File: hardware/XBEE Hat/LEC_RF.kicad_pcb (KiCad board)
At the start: 2 copper layers, 70 x 40 mm, 6 parts, among them J1 Conn_Coaxial_Small, J2 Conn_01x04, U1 XBee_SMT, U2 TLV1117-33

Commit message: Push of most recent schematic and PCB
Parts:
- C1, C2: footprint Capacitor_SMD:C_0805_2012Metric -> Capacitor_SMD:C_0603_1608Metric
- U1: footprint RF_Module:Digi_XBee_SMT -> Custom:XBEE_GND_PAD
- moved J2 11.1 mm to (84.3, 85.0)
- moved U2 10.3 mm to (86.0, 66.0)
- moved C1 2.70 mm to (125.2, 62.0)
- moved C2 2.00 mm to (128.1, 62.0)
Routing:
- net UART_TX: track 0.00 -> 51.1 mm, vias 0 -> 1
- net UART_RX: track 0.00 -> 47.4 mm
- net +3.3V: track 9.13 -> 54.2 mm
- net +5V: track 0.00 -> 9.89 mm
- net Net-(J1-In): track 0.00 -> 7.13 mm
- added copper zone on B.Cu, net GND
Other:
- board size 70 x 40 mm -> 60 x 40 mm

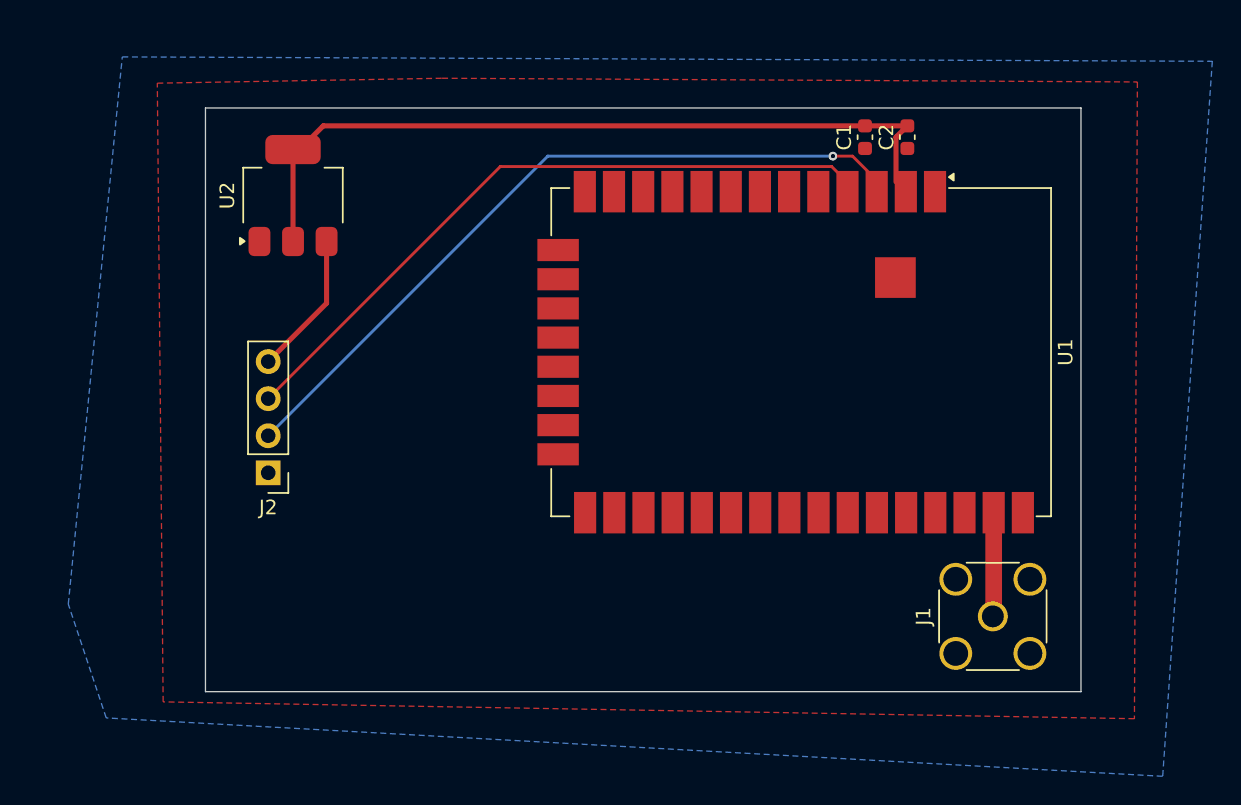
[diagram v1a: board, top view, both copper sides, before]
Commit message: Routed XBEE PCB
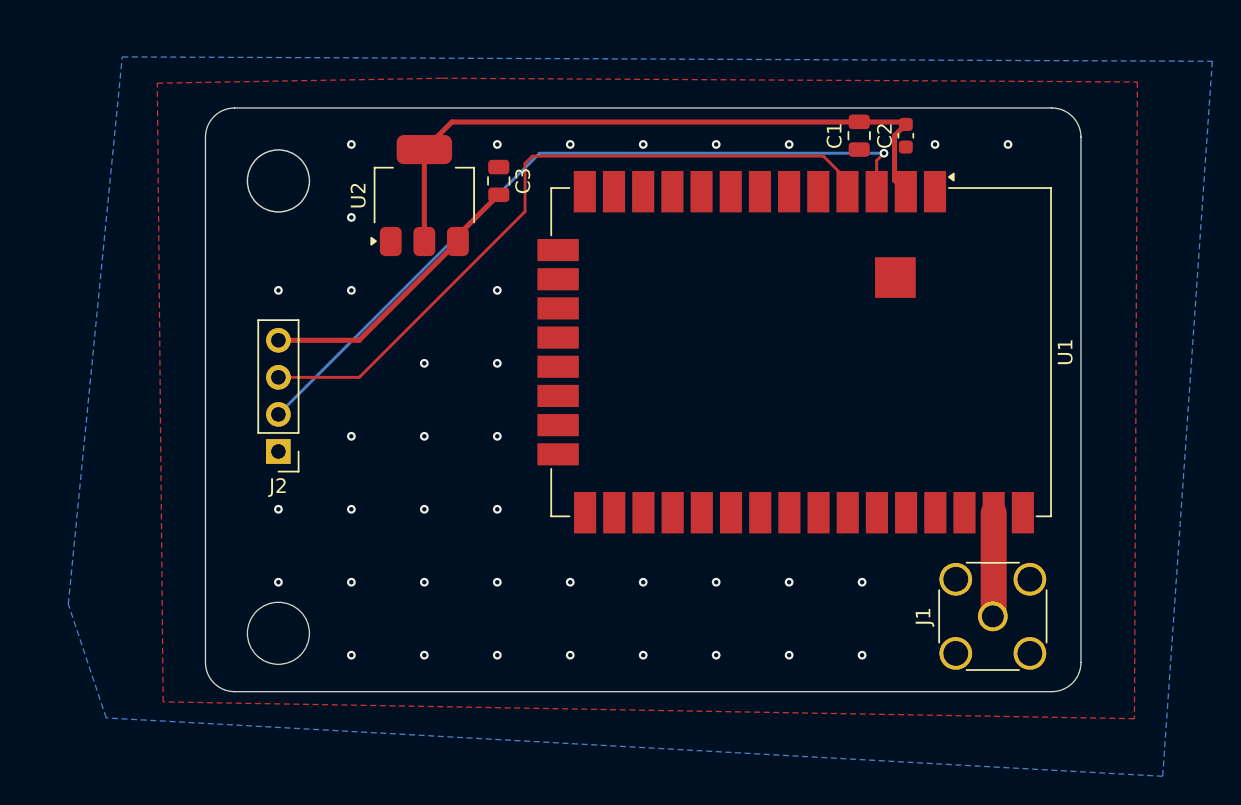
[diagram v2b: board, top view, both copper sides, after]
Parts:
- added C3: 1uF, Capacitor_SMD:C_0805_2012Metric, F.Cu at (100.1, 65.0)
- C1: footprint Capacitor_SMD:C_0603_1608Metric -> Capacitor_SMD:C_0805_2012Metric
- U2: value TLV1117-33 -> TLV1117LV33DCYR
- moved U2 9.00 mm to (95.0, 66.0)
- moved J2 1.62 mm to (85.0, 83.5)
- moved C1 0.41 mm to (124.8, 61.9)
- moved C2 0.14 mm to (128.0, 61.9)
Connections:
- net UART_RX renamed /UART_RX
- net UART_TX renamed /UART_TX
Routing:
- net +5V: track 9.89 -> 19.5 mm
- net +3.3V: track 54.2 -> 45.4 mm
- net /UART_RX: track 47.4 -> 48.7 mm
- net /UART_TX: track 51.1 -> 51.8 mm
- net GND: vias 0 -> 38
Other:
- outline, holes or cut-outs redrawn

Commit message: Final revision of XBEE board
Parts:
- removed J1: Conn_Coaxial_Small, Connector_Coaxial:SMA_Wurth_60312002114503_Vertical
- added C4: 1nF, Capacitor_SMD:C_0805_2012Metric, F.Cu at (117.5, 62.2)
- added R1: 300, Resistor_SMD:R_0805_2012Metric, F.Cu at (112.8, 62.2)
- added REF**: MountingHole_3.2mm_M3, MountingHole:MountingHole_3.2mm_M3, F.Cu at (85.0, 65.0)
- added REF**: MountingHole_3.2mm_M3, MountingHole:MountingHole_3.2mm_M3, F.Cu at (85.0, 95.0)
- added REF**: MountingHole_3.2mm_M3, MountingHole:MountingHole_3.2mm_M3, F.Cu at (121.0, 95.0)
- moved U1 1.26 mm to (120.1, 78.0)
- moved C1 0.58 mm to (124.3, 62.2), turned to 0 degrees
- turned C2 to 180 degrees
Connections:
- C1 pad 2: +3.3V -> VCC
- C2 pad 2: +3.3V -> VCC
- U1 pad 2: +3.3V -> VCC
- U1 pad 36: Net-(J1-In) -> unconnected-(U1-RF-Pad36)
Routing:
- net +3.3V: track 45.4 -> 23.8 mm
- net VCC: track 0.00 -> 20.7 mm
- net Net-(J1-In): track 7.13 -> 0.00 mm
- net /UART_RX: track 48.7 -> 45.9 mm, vias 0 -> 2
- net GND: vias 38 -> 185
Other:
- outline, holes or cut-outs redrawn
- board text added: "{ "ViaStitching": "0.2", "stitch_zone_0": { "HSpacing": "0.7", "VSpacing": "0.7", "HOffset": "0", "VOffset": "0", "Clearance": "0", "Randomize": false } }"
- board text added: "{ "ViaStitching": "0.2", "stitch_zone_0": { "HSpacing": "1", "VSpacing": "1", "HOffset": "0", "VOffset": "0", "Clearance": "0", "Randomize": false } }"
- board text added: "{ "ViaStitching": "0.2", "stitch_zone_0": { "HSpacing": "1", "VSpacing": "1", "HOffset": "0", "VOffset": "0", "Clearance": "0", "Randomize": true } }"
- board text added: "{ "ViaStitching": "0.2", "stitch_zone_0": { "HSpacing": "1", "VSpacing": "1", "HOffset": "0", "VOffset": "0", "Clearance": "0.2", "Randomize": false } }"
- board text added: "{ "ViaStitching": "0.2", "stitch_zone_0": { "HSpacing": "1", "VSpacing": "1", "HOffset": "0", "VOffset": "0", "Clearance": "1", "Randomize": false } }"
- board text added: "{ "ViaStitching": "0.2", "stitch_zone_0": { "HSpacing": "2", "VSpacing": "2", "HOffset": "0", "VOffset": "0", "Clearance": "0.5", "Randomize": false } }"
- board text added: "{ "ViaStitching": "0.2", "stitch_zone_0": { "HSpacing": "2", "VSpacing": "2", "HOffset": "0", "VOffset": "0", "Clearance": "1.5", "Randomize": false } }"

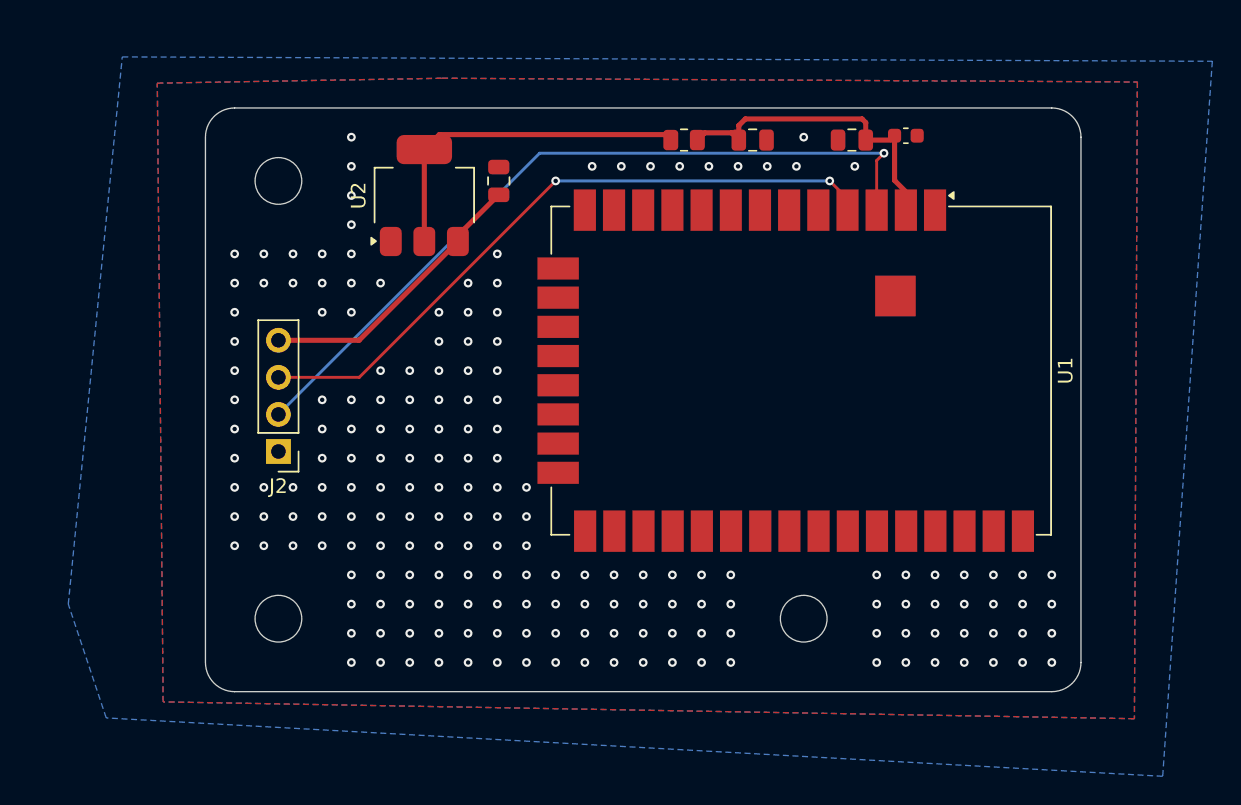
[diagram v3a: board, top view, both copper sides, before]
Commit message: Experimenting with alternate layout bc no SMA connector
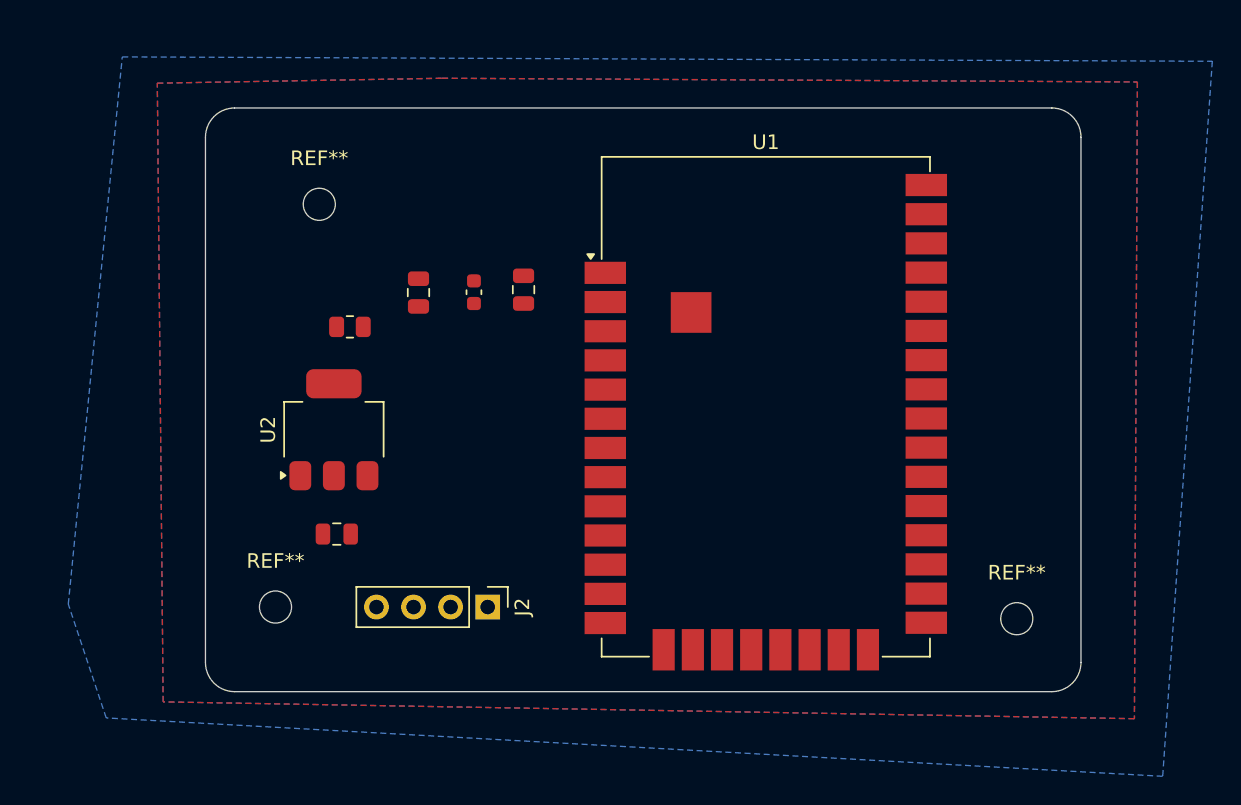
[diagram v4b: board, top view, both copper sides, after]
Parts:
- removed the REF** at (85.0, 65.0)
- removed the REF** at (85.0, 95.0)
- removed the REF** at (121.0, 95.0)
- added REF**: MountingHole_2.2mm_M2, MountingHole:MountingHole_2.2mm_M2, F.Cu at (135.6, 95.0)
- added REF**: MountingHole_2.2mm_M2, MountingHole:MountingHole_2.2mm_M2, F.Cu at (84.8, 94.2)
- added REF**: MountingHole_2.2mm_M2, MountingHole:MountingHole_2.2mm_M2, F.Cu at (87.8, 66.6)
- moved C1 31.5 mm to (94.6, 72.7), turned to -90 degrees
- moved C2 31.5 mm to (98.4, 72.6), turned to -90 degrees
- moved C3 26.6 mm to (89.0, 89.2), turned to 0 degrees
- moved R1 26.2 mm to (89.9, 75.0)
- moved C4 18.7 mm to (101.8, 72.5), turned to -90 degrees
- moved J2 17.9 mm to (99.3, 94.2), turned to -90 degrees
- moved U2 17.2 mm to (88.8, 82.0)
- moved U1 3.62 mm to (118.4, 81.2), turned to 0 degrees
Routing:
- net /UART_TX: track 51.8 -> 0.00 mm, vias 1 -> 0
- net /UART_RX: track 45.9 -> 0.00 mm, vias 2 -> 0
- net +3.3V: track 23.8 -> 0.00 mm
- net VCC: track 20.7 -> 0.00 mm
- net +5V: track 19.1 -> 0.00 mm
- net GND: vias 185 -> 0

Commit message: Routed revised XBEE PCB layout
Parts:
- moved R1 7.98 mm to (97.8, 73.9), turned to 90 degrees
- moved C1 6.03 mm to (100.5, 73.9), turned to 90 degrees
- moved C2 5.85 mm to (103.5, 75.5), turned to 90 degrees
- moved U2 4.61 mm to (86.6, 86.1)
- moved C3 3.96 mm to (91.7, 86.3), turned to -90 degrees
- moved C4 1.76 mm to (103.5, 72.0)
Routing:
- net /UART_TX: track 0.00 -> 23.7 mm, vias 0 -> 2
- net /UART_RX: track 0.00 -> 22.8 mm
- net +3.3V: track 0.00 -> 20.9 mm
- net VCC: track 0.00 -> 11.5 mm
- net +5V: track 0.00 -> 9.75 mm
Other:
- board text added: "{ "ViaStitching": "0.2", "stitch_zone_0": { "HSpacing": "1", "VSpacing": "1", "HOffset": "0", "VOffset": "0", "Clearance": "2", "Randomize": false } }"

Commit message: Done
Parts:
- removed R1: 300, Resistor_SMD:R_0805_2012Metric
- removed U2: TLV1117LV33DCYR, Package_TO_SOT_SMD:SOT-223-3_TabPin2
- added C10: 1u, Capacitor_SMD:C_0805_2012Metric, F.Cu at (100.8, 71.4)
- added C5: 100n, Capacitor_SMD:C_0603_1608Metric, F.Cu at (89.6, 90.0)
- added C6: 100n, Capacitor_SMD:C_0603_1608Metric, F.Cu at (91.1, 84.0)
- added CR1: LD1086DT33TR, Package_TO_SOT_SMD:TO-252-2, F.Cu at (87.6, 74.8)
- added FB1: FerriteBead, Resistor_SMD:R_0603_1608Metric, F.Cu at (90.2, 87.0)
- added G***: LOGO, RDT_Logo:RDT_Logo, F.Cu at (98.7, 84.8)
- C1: value 1uF -> 22uF
- C2: value 100nF -> 10u; footprint Capacitor_SMD:C_0603_1608Metric -> Capacitor_SMD:C_1210_3225Metric
- C3: value 1uF -> 10uF
- C4: value 1nF -> 100n; footprint Capacitor_SMD:C_0805_2012Metric -> Capacitor_SMD:C_0603_1608Metric
- U1: value XBee_SMT -> XBP9X-DMUS-001
- moved C1 8.57 mm to (93.0, 69.8)
- moved C3 5.37 mm to (87.5, 83.0), turned to 180 degrees
- moved C2 4.81 mm to (98.8, 76.7), turned to -90 degrees
- moved REF** 1.80 mm to (86.3, 65.6)
- moved C4 0.07 mm to (103.5, 72.0)
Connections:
- C1 pad 1: GND -> VCC
- C1 pad 2: VCC -> GND
- C2 pad 1: GND -> VCC
- C2 pad 2: VCC -> GND
- C3 pad 1: GND -> +5V_Filt
- C3 pad 2: +5V -> GND
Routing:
- net +3.3V: track 20.9 -> 0.00 mm
- net VCC: track 11.5 -> 0.00 mm
- net +5V: track 9.75 -> 0.00 mm
- net /UART_RX: track 22.8 -> 25.3 mm
- net /UART_TX: track 23.7 -> 24.3 mm
- net GND: vias 0 -> 129
- added copper zone on F.Cu, net +5V
- added copper zone on F.Cu, net +5V_Filt
- added copper zone on F.Cu, net VCC
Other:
- board text added: "+5V"
- board text added: "Board: XBee Module Designer: Jacob Schroll Designed: 11/2025"
- board text added: "GND"
- board text added: "Rx"
- board text added: "Tx"
- board text added: "Vcc (3.3V)"
- board text added: "XBee-Pro SX 900 1W"
- board text added: "{ "ViaStitching": "0.2", "stitch_zone_0": { "HSpacing": "1.2", "VSpacing": "1.2", "HOffset": "0", "VOffset": "0", "Clearance": "1.2", "Randomize": false } }"
- board text added: "{ "ViaStitching": "0.2", "stitch_zone_0": { "HSpacing": "1.4", "VSpacing": "1.4", "HOffset": "0", "VOffset": "0", "Clearance": "1.4", "Randomize": false } }"
- board text added: "{ "ViaStitching": "0.2", "stitch_zone_0": { "HSpacing": "2", "VSpacing": "2", "HOffset": "0", "VOffset": "0", "Clearance": "2", "Randomize": false } }"
- board text added: "{ "ViaStitching": "0.2", "stitch_zone_0": { "HSpacing": "3", "VSpacing": "3", "HOffset": "0", "VOffset": "0", "Clearance": "3", "Randomize": false } }"

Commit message: Finished PCBs
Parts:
- moved C1 0.50 mm to (93.5, 69.8)
- moved C5 0.40 mm to (89.2, 90.0)
- moved C6 0.12 mm to (91.2, 84.0)
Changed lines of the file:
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@@
 			(plot_on_all_layers_selection 0x00000000_00000000_00000000_00000000)
 			(disableapertmacros no)
-			(usegerberextensions no)
-			(usegerberattributes yes)
-			(usegerberadvancedattributes yes)
-			(creategerberjobfile yes)
+			(usegerberextensions yes)
+			(usegerberattributes no)
+			(usegerberadvancedattributes no)
+			(creategerberjobfile no)
 			(dashed_line_dash_ratio 12.000000)
 			(dashed_line_gap_ratio 3.000000)
@@
 			(sketchdnponfab yes)
 			(crossoutdnponfab yes)
-			(subtractmaskfromsilk no)
+			(subtractmaskfromsilk yes)
 			(outputformat 1)
 			(mirror no)
 			(drillshape 0)
 			(scaleselection 1)
-			(outputdirectory "../LEC PCB/")
+			(outputdirectory "gerbers/")
 		)
 	)
@@
 	(footprint "Capacitor_SMD:C_0805_2012Metric"
 		(layer "F.Cu")
-		(at 92.95 69.85 90)
+		(at 93.45 69.8 90)
 		(descr "Capacitor SMD 0805 (2012 Metric), square (rectangular) end terminal, IPC-7351 nominal, (Body size source: IPC-SM-782 page 76, https://www.pcb-3d.com/wordpress/wp-content/uploads/ipc-sm-782a_amendment_1_and_2.pdf, https://docs.google.com/spreadsheets/d/1BsfQQcO9C6DZCsRaXUlFlo91Tg2WpOkGARC1WS5S8t0/edit?usp=sharing), generated with kicad-footprint-generator")
 		(tags "capacitor")
 		(property "Reference" "C1"
-			(at 2.65 0.15 0)
+			(at 2.6 -0.1 0)
 			(layer "F.SilkS")
 			(effects
@@
 			)
 		)
+		(property "DigiKey" "https://www.digikey.com/en/products/detail/digi/XBP9X-DMUS-001/5972744"
+			(at 0 0 0)
+			(unlocked yes)
+			(layer "F.Fab")
+			(hide yes)
+			(effects
+				(font
+					(size 1 1)
+					(thickness 0.15)
+				)
+			)
+		)
 		(property ki_fp_filters "Digi*XBee*SMT*")
 		(sheetname "/")
@@
 	(footprint "Capacitor_SMD:C_0603_1608Metric"
 		(layer "F.Cu")
-		(at 89.6 90)
+		(at 89.2 90)
 		(descr "Capacitor SMD 0603 (1608 Metric), square (rectangular) end terminal, IPC-7351 nominal, (Body size source: IPC-SM-782 page 76, https://www.pcb-3d.com/wordpress/wp-content/uploads/ipc-sm-782a_amendment_1_and_2.pdf), generated with kicad-footprint-generator")
 		(tags "capacitor")
@@
 	(footprint "Capacitor_SMD:C_0603_1608Metric"
 		(layer "F.Cu")
-		(at 91.075 84 180)
+		(at 91.2 84 180)
 		(descr "Capacitor SMD 0603 (1608 Metric), square (rectangular) end terminal, IPC-7351 nominal, (Body size source: IPC-SM-782 page 76, https://www.pcb-3d.com/wordpress/wp-content/uploads/ipc-sm-782a_amendment_1_and_2.pdf), generated with kicad-footprint-generator")
 		(tags "capacitor")
